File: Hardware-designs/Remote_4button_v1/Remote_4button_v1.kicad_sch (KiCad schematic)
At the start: 34 parts, among them J1 UART, J2 Bat, J3 USB_C, J4 Conn_01x08_Pin, SW1 PTS526 SM15 SMTR2 LFS, SW2 PTS526 SM15 SMTR2 LFS, SW3 PTS526 SM15 SMTR2 LFS, SW4 PTS526 SM15 SMTR2 LFS, SW5 PTS526 SM15 SMTR2 LFS, U1 ESP32-WROOM-32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

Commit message: Add pcb images, step file, and pdf schematic for all hardware designs.
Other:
- title: (none) -> HueMix-Link 4-Button Remote
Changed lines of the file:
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@@
 	(generator_version "9.0")
 	(paper "A4")
+	(title_block
+		(title "HueMix-Link 4-Button Remote")
+		(date "2026-02-18")
+		(rev "1.0")
+	)
 	(junction
 		(at 138.43 133.35)

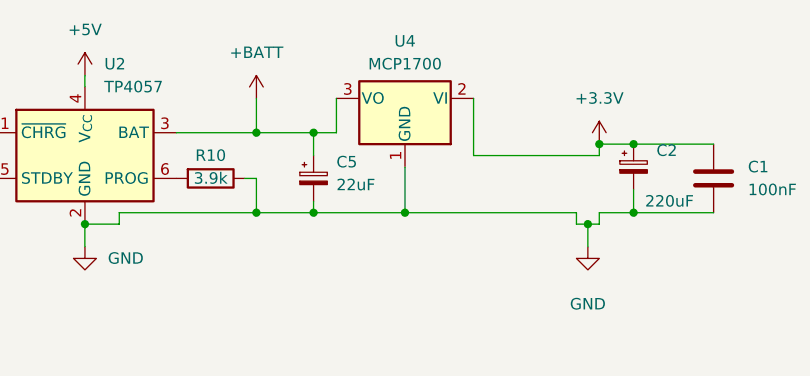
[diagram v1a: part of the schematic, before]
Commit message: correction voltage regulator
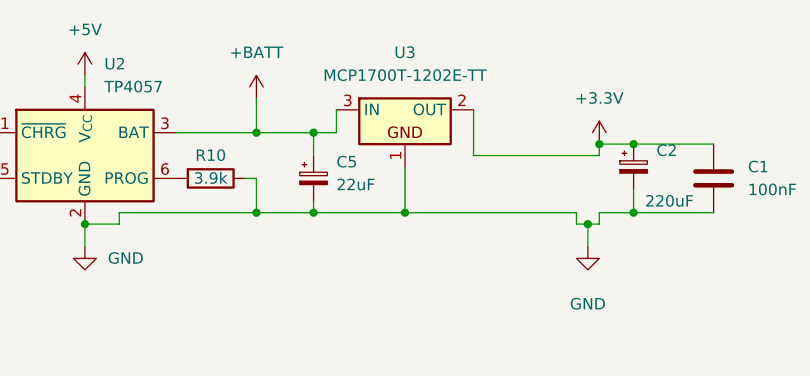
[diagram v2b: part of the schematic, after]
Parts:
- removed U4: MCP1700, MCP1700T_3302E_TT 3:SOT-23_MC_MCH, symbol Regulator_Linear:MCP1700-3302E_TO92
- added U3: MCP1700T-1202E-TT, PCM_Package_TO_SOT_SMD_AKL:SOT-23, symbol PCM_Voltage_Regulator_AKL:MCP1700T-1202E-TT
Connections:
- net +3.3V: now also U3.2 (OUT)
- net +BATT: now also U3.3 (IN)
- net GND: now also U3.1
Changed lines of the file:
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@@
 	(wire
 		(pts
+			(xy 203.2 25.4) (xy 203.2 30.48)
+		)
+		(stroke
+			(width 0)
+			(type default)
+		)
+	)
+	(wire
+		(pts
 			(xy 118.11 148.59) (xy 118.11 160.02)
 		)
@@
 	(wire
 		(pts
-			(xy 187.96 27.94) (xy 187.96 24.13)
+			(xy 187.96 27.94) (xy 187.96 25.4)
 		)
 		(stroke
@@
 	(wire
 		(pts
-			(xy 203.2 30.48) (xy 203.2 24.13)
-		)
-		(stroke
-			(width 0)
-			(type default)
-		)
-	)
-	(wire
-		(pts
 			(xy 181.61 74.93) (xy 185.42 74.93)
 		)
@@
 	)
 	(symbol
-		(lib_id "Regulator_Linear:MCP1700-3302E_TO92")
-		(at 195.58 24.13 180)
-		(unit 1)
-		(exclude_from_sim no)
-		(in_bom yes)
-		(on_board yes)
-		(dnp no)
-		(fields_autoplaced yes)
-		(property "Reference" "U4"
-			(at 195.58 17.78 0)
-			(effects
-				(font
-					(size 1.27 1.27)
-				)
-			)
-		)
-		(property "Value" "MCP1700"
-			(at 195.58 20.32 0)
-			(effects
-				(font
-					(size 1.27 1.27)
-				)
-			)
-		)
-		(property "Footprint" "MCP1700T_3302E_TT 3:SOT-23_MC_MCH"
-			(at 195.58 19.05 0)
-			(effects
-				(font
-					(size 1.27 1.27)
-					(italic yes)
-				)
-				(hide yes)
-			)
-		)
-		(property "Datasheet" "http://ww1.microchip.com/downloads/en/DeviceDoc/20001826D.pdf"
-			(at 195.58 24.13 0)
-			(effects
-				(font
-					(size 1.27 1.27)
-				)
-				(hide yes)
-			)
-		)
-		(property "Description" ""
-			(at 195.58 24.13 0)
-			(effects
-				(font
-					(size 1.27 1.27)
-				)
-			)
-		)
-		(pin "1"
-		)
-		(pin "2"
-		)
-		(pin "3"
-		)
-		(instances
-			(project "esp_now_button_3.1"
-				(path "/0f0498d4-a5c0-4d85-9217-2613ef2d2837"
-					(reference "U4")
-					(unit 1)
-				)
-			)
-		)
-	)
-	(symbol
 		(lib_id "power:+3.3V")
 		(at 116.84 119.38 0)
@@
 					(unit 1)
 				)
+			)
+		)
+	)
+	(symbol
+		(lib_id "PCM_Voltage_Regulator_AKL:MCP1700T-1202E-TT")
+		(at 195.58 25.4 0)
+		(unit 1)
+		(exclude_from_sim no)
+		(in_bom yes)
+		(on_board yes)
+		(dnp no)
+		(fields_autoplaced yes)
+		(property "Reference" "U3"
+			(at 195.58 19.05 0)
+			(effects
+				(font
+					(size 1.27 1.27)
+				)
+			)
+		)
+		(property "Value" "MCP1700T-1202E-TT"
+			(at 195.58 21.59 0)
+			(effects
+				(font
+					(size 1.27 1.27)
+				)
+			)
+		)
+		(property "Footprint" "PCM_Package_TO_SOT_SMD_AKL:SOT-23"
+			(at 195.58 25.4 0)
+			(effects
+				(font
+					(size 1.27 1.27)
+				)
+				(hide yes)
+			)
+		)
+		(property "Datasheet" "https://ww1.microchip.com/downloads/en/DeviceDoc/MCP1700-Low-Quiescent-Current-LDO-20001826E.pdf"
+			(at 195.58 25.4 0)
+			(effects
+				(font
+					(size 1.27 1.27)
+				)
+				(hide yes)
+			)
+		)
+		(property "Description" "SOT-23 1.2V 200mA Low dropout 3-terminal voltage regulator, Alternate KiCad Library"
+			(at 195.58 25.4 0)
+			(effects
+				(font
+					(size 1.27 1.27)
+				)
+				(hide yes)
+			)
+		)
+		(pin "3"
+		)
+		(pin "2"
+		)
+		(pin "1"
+		)
+		(instances
+			(project ""
+				(path "/0f0498d4-a5c0-4d85-9217-2613ef2d2837"
+					(reference "U3")
+					(unit 1)
+				)

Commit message: Minor KiCad files update for all devices
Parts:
- C3: value 1nF -> 68nF
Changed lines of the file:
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@@
 			)
 		)
-		(property "Value" "1nF"
+		(property "Value" "68nF"
 			(at 25.4 40.6399 0)
 			(effects
